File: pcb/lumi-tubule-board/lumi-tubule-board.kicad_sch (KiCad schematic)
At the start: 17 parts, among them U2 VREG_SOT23-5, U3 ESP32-S3-MINI-1

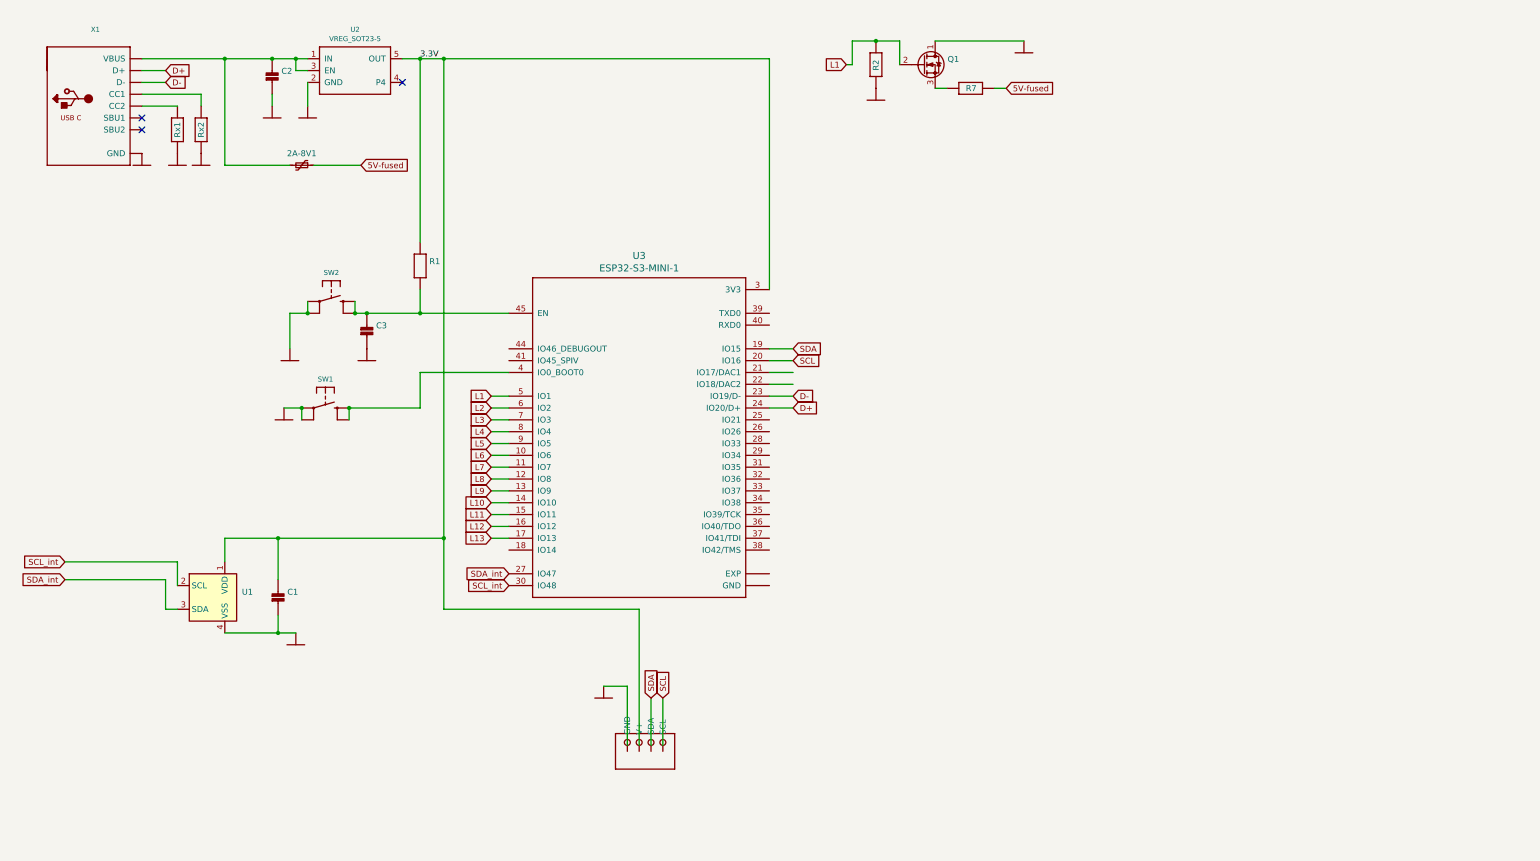
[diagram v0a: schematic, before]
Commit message: Fix schematic footprint issues
Fixed footprint errors in pcbnew. Initial exploration of layout. Fixed typo in banner.
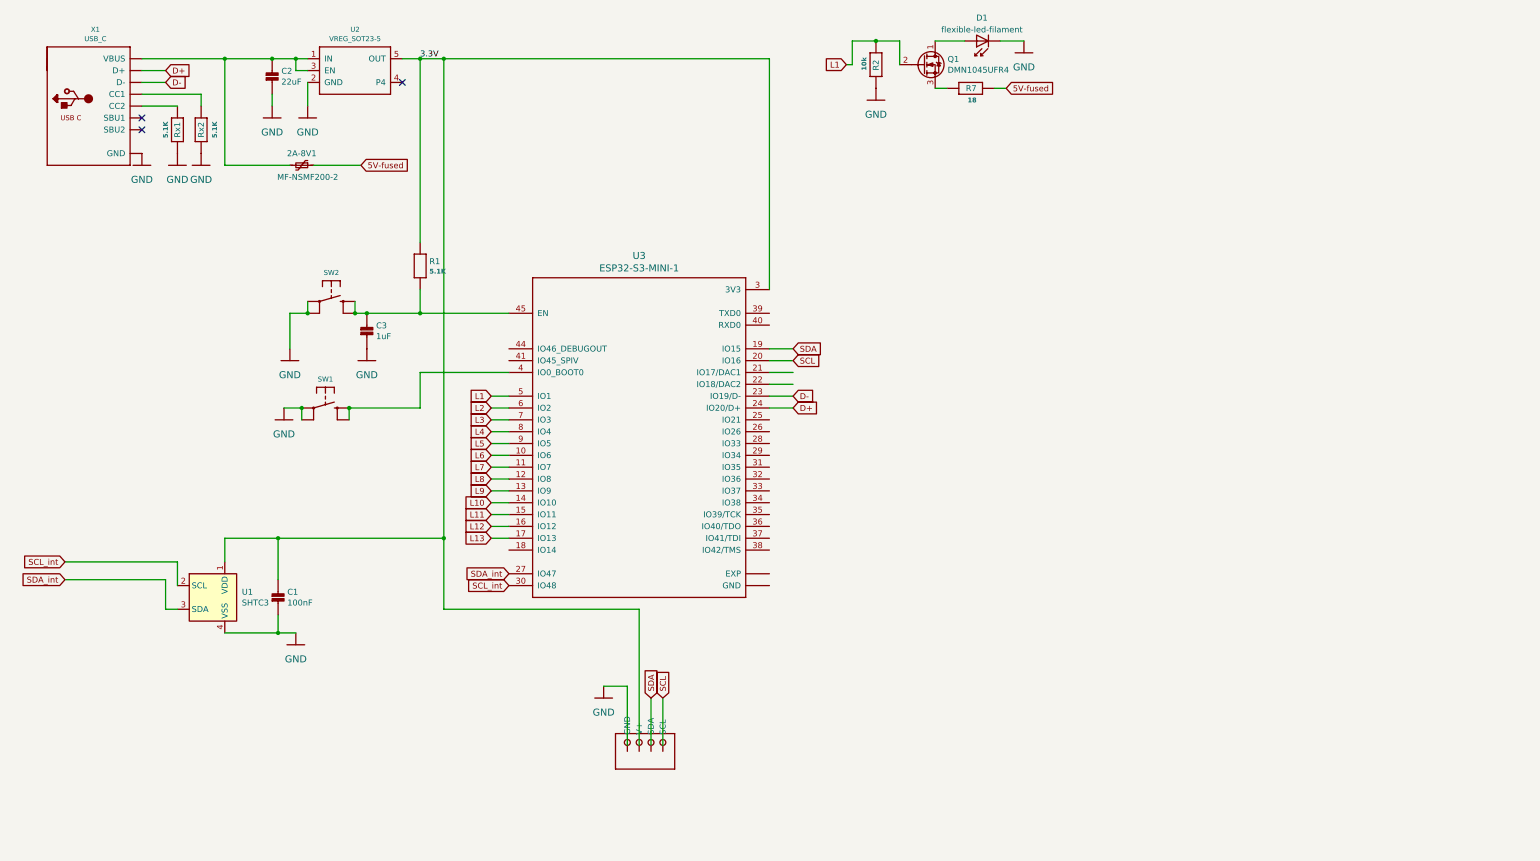
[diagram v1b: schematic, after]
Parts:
- added D1: flexible-led-filament, lumi-tubule-board:Flexible LED filament viamount, symbol lumi-tubule-board:flexible-led-filament
- 2A-8V1: value (none) -> MF-NSMF200-2; footprint (none) -> lumi-tubule-board:MF-NSMF200-2
- C1: value (none) -> 100nF; footprint (none) -> Capacitor_SMD:C_0805_2012Metric
- C2: value (none) -> 22uF; footprint (none) -> Capacitor_SMD:C_0603_1608Metric
- C3: value (none) -> 1uF; footprint (none) -> Capacitor_SMD:C_1206_3216Metric
- Q1: value (none) -> DMN1045UFR4; footprint (none) -> lumi-tubule-board:DMN1045UFR4
- R1, Rx1, Rx2: value (none) -> 5.1K; footprint (none) -> Resistor_SMD:R_0805_2012Metric
- R2: value (none) -> 10k; footprint (none) -> Resistor_SMD:R_1206_3216Metric
- R7: value (none) -> 18; footprint (none) -> Resistor_SMD:R_1206_3216Metric
- SW1, SW2: value (none) -> SWITCH_TACT_SMT4.6X2.8; footprint (none) -> lumi-tubule-board:BTN_KMR2_4.6X2.8
- U1: value (none) -> SHTC3; footprint (none) -> Sensor_Humidity:Sensirion_DFN-4-1EP_2x2mm_P1mm_EP0.7x1.6mm
- X1: value (none) -> USB_C; footprint (none) -> Connector_USB:USB_C_Receptacle_HRO_TYPE-C-31-M-12
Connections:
- net GND: now also X1.A1 (GND), X1.A12 (GND), X1.B1 (GND), X1.B12 (GND), D1.1 (K); no longer Q1.1 (Drain), X1.A1B12 (GND), X1.B1A12 (GND)
- net at 2A-8V1.2, C2.1, U2.1 (IN)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: now also X1.A4 (VBUS), X1.A9 (VBUS), X1.B4 (VBUS), X1.B9 (VBUS); no longer X1.A4B9 (VBUS), X1.B4A9 (VBUS)
- new net: D1.2 (A), Q1.1 (Drain)

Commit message: PCB design update
Added LIS2DH12 accelerometer to PCB. Reworked the filament pads. Fixed footprints. Added pullup resistors to I2C lines. Started planning the layout in more compact footprint.
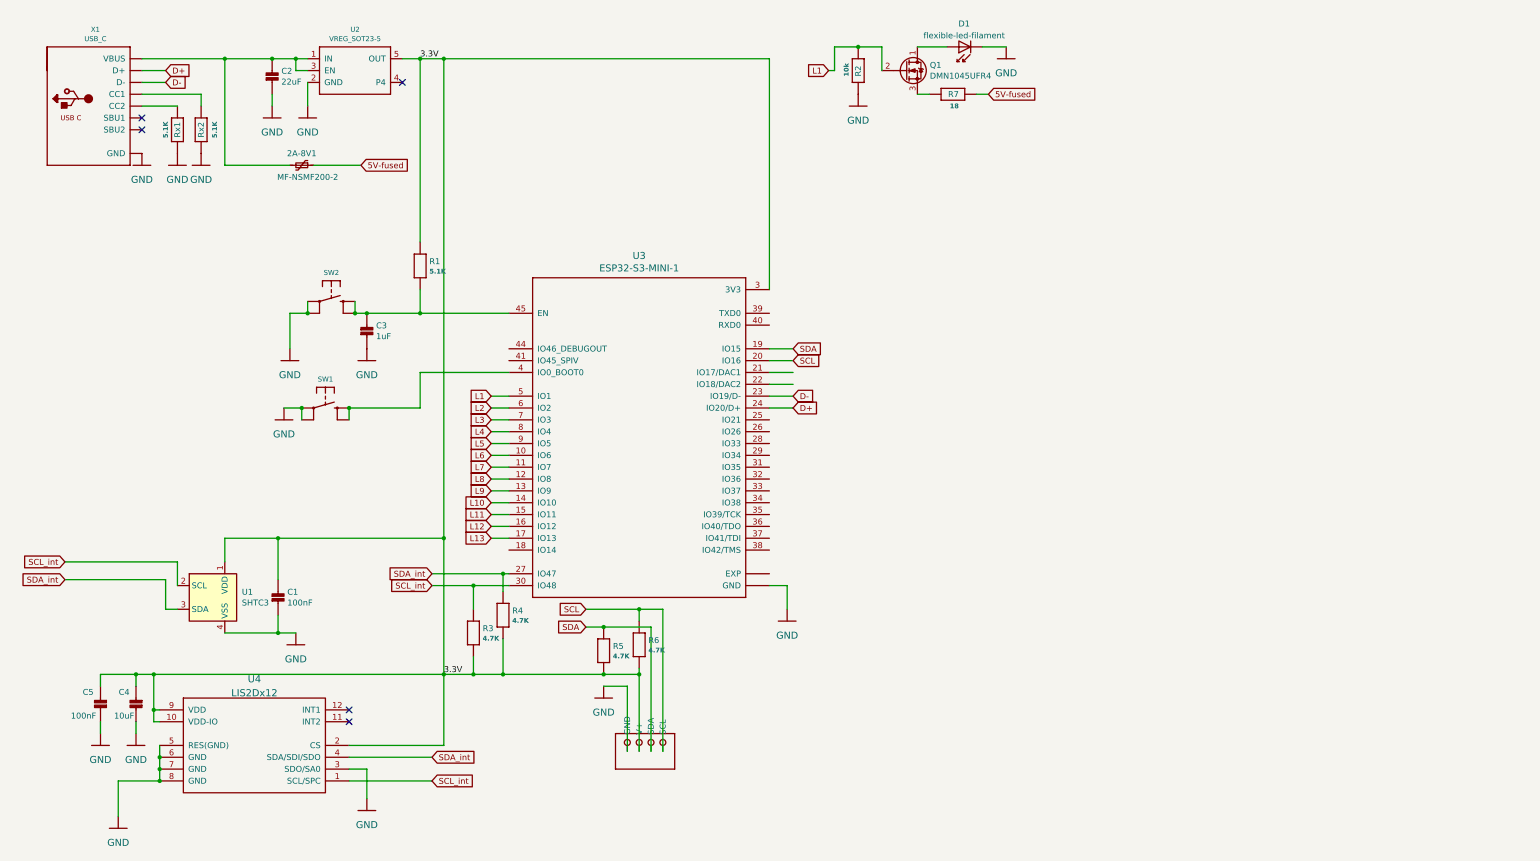
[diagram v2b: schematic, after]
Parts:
- added C4: 10uF, Capacitor_SMD:C_0805_2012Metric, symbol Adafruit_ESP32-S3_8MB_No_PSRAM-eagle-import:CAP_CERAMIC_0402
- added C5: 100nF, Capacitor_SMD:C_0402_1005Metric, symbol Adafruit_ESP32-S3_8MB_No_PSRAM-eagle-import:CAP_CERAMIC_0402
- added R3, R4, R5, R6: 4.7K, Resistor_SMD:R_0603_1608Metric, symbol Adafruit_ESP32-S3_8MB_No_PSRAM-eagle-import:RESISTOR_0603_NOOUT
- added U4: LIS2Dx12, Package_LGA:LGA-12_2x2mm_P0.5mm, symbol lumi-tubule-board:LIS2Dx12
- U2: JLCPCB ref (none) -> C176944
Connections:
- net 3.3V: now also CONN1.2 (V+), C4.2, C5.2, R3.2, R4.2, R5.2, R6.2, U4.10 (VDD-IO), U4.2 (CS), U4.9 (VDD)
- net GND: now also CONN1.1 (GND), U3.1 (GND), U3.2 (GND), U3.42 (GND), U3.43 (GND), U3.46 (GND), U3.47 (GND), U3.48 (GND), U3.49 (GND), U3.50 (GND), U3.51 (GND), U3.52 (GND), U3.53 (GND), U3.54 (GND), U3.55 (GND), U3.56 (GND), U3.57 (GND), U3.58 (GND), U3.59 (GND), U3.60 (GND), U3.62 (GND), U3.63 (GND), U3.64 (GND), U3.65 (GND), C4.1, C5.1, U4.3 (SDO/SA0), U4.5 (RES(GND)), U4.6 (GND), U4.7 (GND), U4.8 (GND)
- net SCL: now also CONN1.4 (SCL), R6.1
- net SCL_int: now also R3.1, U4.1 (SCL/SPC)
- net SDA: now also CONN1.3 (SDA), R5.1
- net SDA_int: now also R4.1, U4.4 (SDA/SDI/SDO)
- no-connect marks 3 -> 5
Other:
- moved on the sheet: D1, Q1, R2, R7

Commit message: Revise PCB
- fixed backwards USB port
- redo power routing
- make I2C lines cleaner
- make differential lines length matched
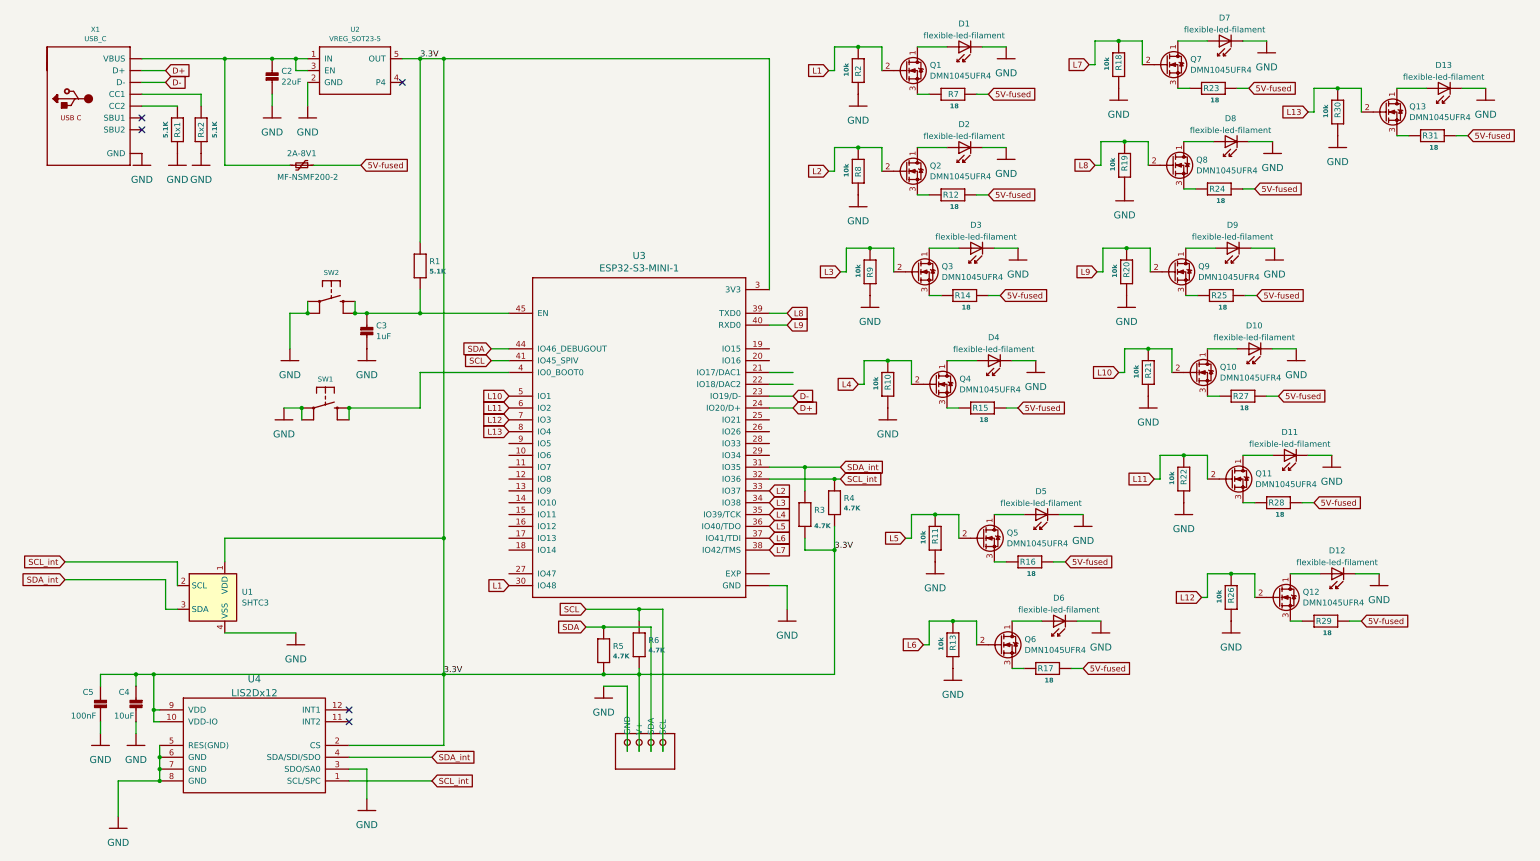
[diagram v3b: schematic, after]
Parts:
- removed C1: 100nF, Capacitor_SMD:C_0805_2012Metric, symbol Adafruit_ESP32-S3_8MB_No_PSRAM-eagle-import:CAP_CERAMIC_0402NO
- added D10, D11, D12, D13, D2, D3, D4, D5, D6, D7, D8, D9: flexible-led-filament, lumi-tubule-board:Flexible LED filament viamount, symbol lumi-tubule-board:flexible-led-filament
- added Q10, Q11, Q12, Q13, Q2, Q3, Q4, Q5, Q6, Q7, Q8, Q9: DMN1045UFR4, lumi-tubule-board:DMN1045UFR4, symbol other-parts:DMN1045UFR4
- added R10, R11, R13, R18, R19, R20, R21, R22, R26, R30, R8, R9: 10k, Resistor_SMD:R_1206_3216Metric, symbol Adafruit_ESP32-S3_8MB_No_PSRAM-eagle-import:RESISTOR_0603_NOOUT
- added R12, R14, R15, R16, R17, R23, R24, R25, R27, R28, R29, R31: 18, Resistor_SMD:R_1206_3216Metric, symbol Adafruit_ESP32-S3_8MB_No_PSRAM-eagle-import:RESISTOR_0603_NOOUT
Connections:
- net 5V-fused: now also R12.1, R14.1, R15.1, R16.1, R17.1, R23.1, R24.1, R25.1, R27.1, R28.1, R29.1, R31.1
- net GND: now also D10.1 (K), D11.1 (K), D12.1 (K), D13.1 (K), D2.1 (K), D3.1 (K), D4.1 (K), D5.1 (K), D6.1 (K), D7.1 (K), D8.1 (K), D9.1 (K), R10.1, R11.1, R13.1, R18.1, R19.1, R20.1, R21.1, R22.1, R26.1, R30.1, R8.1, R9.1
- net L1: now also U3.30 (IO48); no longer U3.5 (IO1)
- net L10: now also U3.5 (IO1), Q10.2 (Gate), R21.2; no longer U3.14 (IO10)
- net L11: now also U3.6 (IO2), Q11.2 (Gate), R22.2; no longer U3.15 (IO11)
- net L12: now also U3.7 (IO3), Q12.2 (Gate), R26.2; no longer U3.16 (IO12)
- net L13: now also U3.8 (IO4), Q13.2 (Gate), R30.2; no longer U3.17 (IO13)
- net L2: now also U3.33 (IO37), Q2.2 (Gate), R8.2; no longer U3.6 (IO2)
- net L3: now also U3.34 (IO38), Q3.2 (Gate), R9.2; no longer U3.7 (IO3)
- net L4: now also U3.35 (IO39/TCK), Q4.2 (Gate), R10.2; no longer U3.8 (IO4)
- net L5: now also U3.36 (IO40/TDO), Q5.2 (Gate), R11.2; no longer U3.9 (IO5)
- net L6: now also U3.37 (IO41/TDI), Q6.2 (Gate), R13.2; no longer U3.10 (IO6)
- net L7: now also U3.38 (IO42/TMS), Q7.2 (Gate), R18.2; no longer U3.11 (IO7)
- net L8: now also U3.39 (TXD0), Q8.2 (Gate), R19.2; no longer U3.12 (IO8)
- net L9: now also U3.40 (RXD0), Q9.2 (Gate), R20.2; no longer U3.13 (IO9)
- net SCL: now also U3.41 (IO45_SPIV); no longer U3.20 (IO16)
- net SCL_int: now also R4.1, U3.32 (IO36); no longer R3.1, U3.30 (IO48)
- net SDA: now also U3.44 (IO46_DEBUGOUT); no longer U3.19 (IO15)
- net SDA_int: now also R3.1, U3.31 (IO35); no longer R4.1, U3.27 (IO47)
- new net: D13.2 (A), Q13.1 (Drain)
- new net: D4.2 (A), Q4.1 (Drain)
- new net: Q4.3 (Source), R15.2
- new net: Q10.3 (Source), R27.2
- new net: D5.2 (A), Q5.1 (Drain)
- new net: Q13.3 (Source), R31.2
- new net: Q5.3 (Source), R16.2
- new net: Q7.3 (Source), R23.2
- new net: Q2.3 (Source), R12.2
- new net: D6.2 (A), Q6.1 (Drain)
- new net: Q8.3 (Source), R24.2
- new net: D3.2 (A), Q3.1 (Drain)
- new net: D8.2 (A), Q8.1 (Drain)
- new net: D9.2 (A), Q9.1 (Drain)
- new net: D10.2 (A), Q10.1 (Drain)
- new net: Q6.3 (Source), R17.2
- new net: D12.2 (A), Q12.1 (Drain)
- new net: Q12.3 (Source), R29.2
- new net: D7.2 (A), Q7.1 (Drain)
- new net: D2.2 (A), Q2.1 (Drain)
- new net: Q3.3 (Source), R14.2
- new net: Q9.3 (Source), R25.2
- new net: D11.2 (A), Q11.1 (Drain)
- new net: Q11.3 (Source), R28.2
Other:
- moved on the sheet: R3, R4
